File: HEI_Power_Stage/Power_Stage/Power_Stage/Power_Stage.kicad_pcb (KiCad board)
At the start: 4 copper layers, 114.7 x 57.4 mm, 151 parts, among them J1 OSTTA020161, J2 Conn_02x10_Odd_Even, J3 Screw_Terminal_01x01, J4 Screw_Terminal_01x01, J5 Screw_Terminal_01x01, Q1 EPC2304ENGRT, Q2 EPC2304ENGRT, Q3 EPC2304ENGRT, Q4 EPC2304ENGRT, Q5 EPC2304ENGRT, Q6 EPC2304ENGRT, T1 30k, T2 30k, T3 30k, T4 30k, T5 30k, T6 30k, U1 TBA 2-1212, U11 NCP51820AMNTWG, U12 ADC124S051CIMM/NOPB, U13 TPS73250DBVR, U14 TPS73250DBVR, U15 ADC124S051CIMM/NOPB, U17 TPS73250DBVR, U2 1769205241, U3 TPS73250DBVR, U5 NCP51820AMNTWG, U6 ADC124S051CIMM/NOPB, U8 NCP51820AMNTWG, U9 ADC124S051CIMM/NOPB

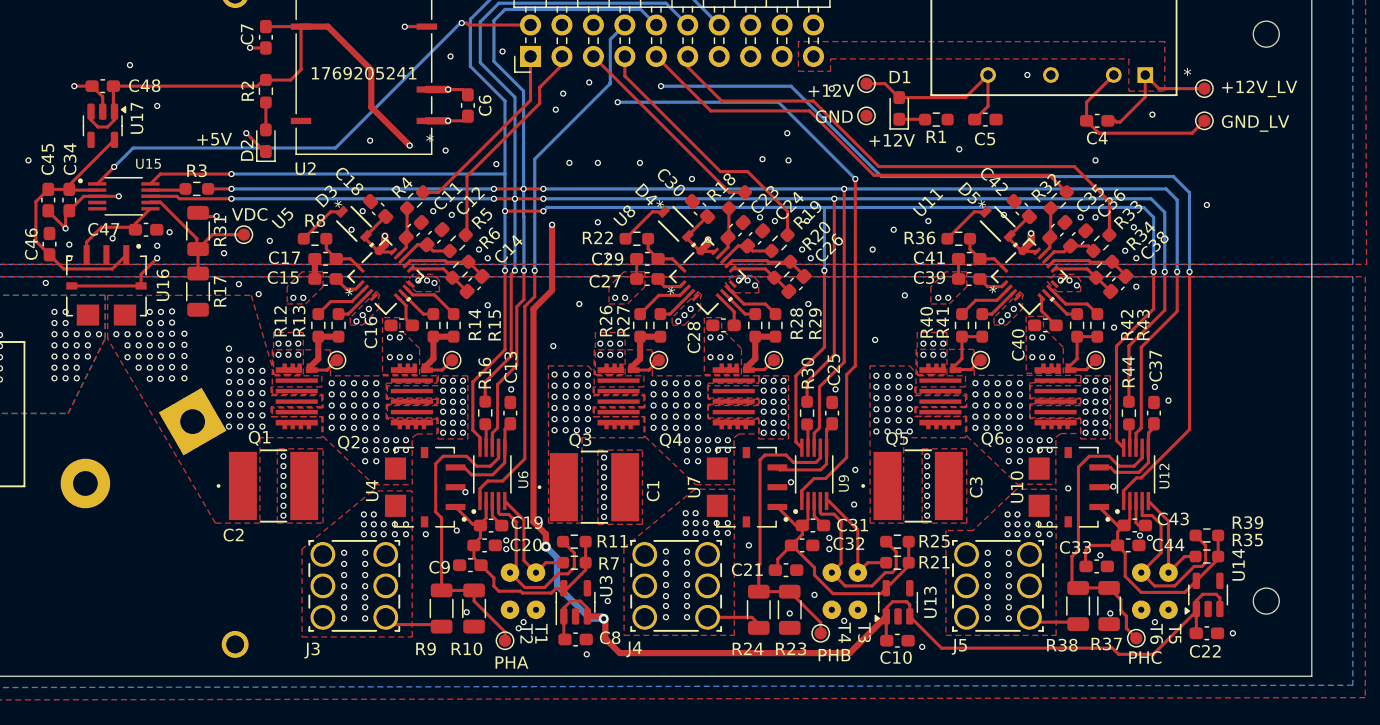
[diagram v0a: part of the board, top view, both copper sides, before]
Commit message: added low pass filters, PGND/SGND jumper
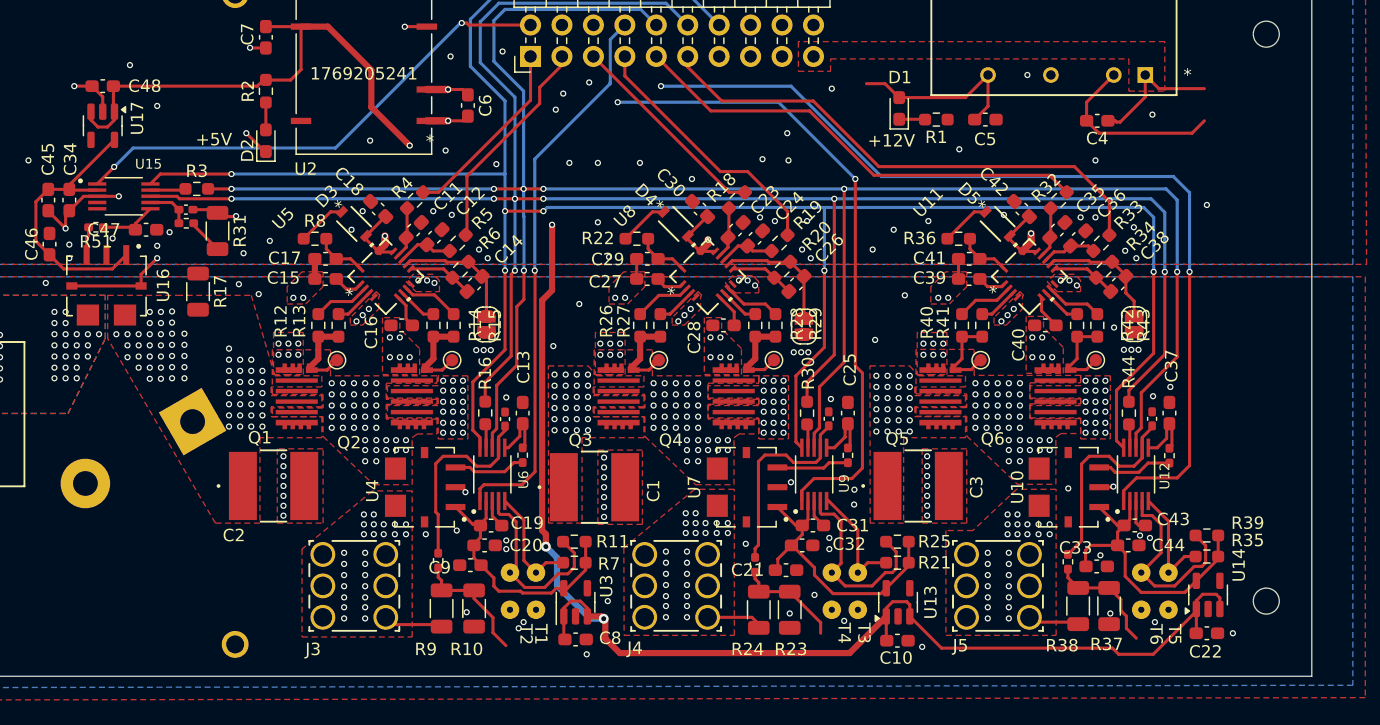
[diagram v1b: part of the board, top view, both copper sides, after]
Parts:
- removed +12V, +12V_LV, GND, GND_LV, PHA, PHB, PHC, VDC: Test_Point, TestPoint:TestPoint_Pad_D1.0mm
- added C54: 15pF, Capacitor_SMD:C_0402_1005Metric_Pad0.74x0.62mm_HandSolder, F.Cu at (126.5, 136.5)
- added C55: 15pF, Capacitor_SMD:C_0402_1005Metric_Pad0.74x0.62mm_HandSolder, F.Cu at (152.7, 136.5)
- added C56: 15pF, Capacitor_SMD:C_0402_1005Metric_Pad0.74x0.62mm_HandSolder, F.Cu at (178.8, 136.5)
- added C63: 15pF, Capacitor_SMD:C_0402_1005Metric_Pad0.74x0.62mm_HandSolder, F.Cu at (100.7, 119.6)
- added JP1: Jumper_2_Open, Jumper:SolderJumper-2_P1.3mm_Open_RoundedPad1.0x1.5mm, F.Cu at (125.0, 128.8)
- added JP2: Jumper_2_Open, Jumper:SolderJumper-2_P1.3mm_Open_RoundedPad1.0x1.5mm, F.Cu at (150.7, 129.0)
- added JP3: Jumper_2_Open, Jumper:SolderJumper-2_P1.3mm_Open_RoundedPad1.0x1.5mm, F.Cu at (177.3, 128.8)
- added R45: 2.2 0.1W, Resistor_SMD:R_0402_1005Metric_Pad0.72x0.64mm_HandSolder, F.Cu at (127.9, 139.4)
- added R46: 2.2 0.1W, Resistor_SMD:R_0402_1005Metric_Pad0.72x0.64mm_HandSolder, F.Cu at (154.2, 139.4)
- added R47: 2.2 0.1W, Resistor_SMD:R_0402_1005Metric_Pad0.72x0.64mm_HandSolder, F.Cu at (180.2, 139.4)
- added R48: 2.2 0.1W, Resistor_SMD:R_0402_1005Metric_Pad0.72x0.64mm_HandSolder, F.Cu at (121.1, 147.9)
- added R49: 2.2 0.1W, Resistor_SMD:R_0402_1005Metric_Pad0.72x0.64mm_HandSolder, F.Cu at (146.7, 148.3)
- added R50: 2.2 0.1W, Resistor_SMD:R_0402_1005Metric_Pad0.72x0.64mm_HandSolder, F.Cu at (172.0, 148.0)
- added R51: 2.2 0.1W, Resistor_SMD:R_0402_1005Metric_Pad0.72x0.64mm_HandSolder, F.Cu at (93.5, 121.0)
- added R57: 2.2 0.1W, Resistor_SMD:R_0402_1005Metric_Pad0.72x0.64mm_HandSolder, F.Cu at (100.8, 120.7)
- moved R31 1.58 mm to (103.3, 121.3)
- moved C25 1.28 mm to (154.2, 136.0)
- moved C37 1.25 mm to (180.2, 136.0)
- moved C13 1.00 mm to (127.9, 136.0)
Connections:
- C13 pad 1: /Phase1/I_{sense} -> /Phase1/I_{ADC}
- C25 pad 1: /Phase2/I_{sense} -> /Phase2/I_{ADC}
- C37 pad 1: /Phase3/I_{sense} -> /Phase3/I_{ADC}
- C46 pad 2: GND -> GNDPWR
- C47 pad 1: /DCI_{sense} -> /I_{DC}
- C47 pad 2: GND -> GNDPWR
- U12 pad 6: /Phase3/I_{sense} -> /Phase3/I_{ADC}
- U12 pad 7: /Phase3/V_{sense} -> /Phase3/V_{ADC}
- U15 pad 6: /DCI_{sense} -> /I_{DC}
- U15 pad 7: /DCV_{sense} -> /V_{DC}
- U16 pad 2: GND -> GNDPWR
- U16 pad 4: GND -> GNDPWR
- U16 pad 7: GND -> GNDPWR
- U6 pad 6: /Phase1/I_{sense} -> /Phase1/I_{ADC}
- U6 pad 7: /Phase1/V_{sense} -> /Phase1/V_{ADC}
- U9 pad 6: /Phase2/I_{sense} -> /Phase2/I_{ADC}
- U9 pad 7: /Phase2/V_{sense} -> /Phase2/V_{ADC}
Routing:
- net /Phase3/V_{ADC}: track 0.00 -> 16.5 mm
- net /Phase2/V_{ADC}: track 0.00 -> 16.4 mm
- net /Phase1/V_{ADC}: track 0.00 -> 16.0 mm
- net /Phase3/V_{sense}: track 24.7 -> 9.43 mm
- net /Phase2/V_{sense}: track 24.3 -> 9.01 mm
- net /Phase1/V_{sense}: track 24.9 -> 10.1 mm
- net GNDPWR: track 28.4 -> 38.9 mm, vias 184 -> 190
- net /DCV_{sense}: track 12.4 -> 2.89 mm
- net /DCI_{sense}: track 7.77 -> 2.30 mm
- net /Phase3/I_{ADC}: track 0.00 -> 5.20 mm
- net /Phase2/I_{ADC}: track 0.00 -> 5.12 mm
- net /I_{DC}: track 0.00 -> 4.88 mm
- net /Phase1/I_{ADC}: track 0.00 -> 4.79 mm
- net /V_{DC}: track 0.00 -> 3.65 mm
- net /Phase1/I_{sense}: track 7.96 -> 5.88 mm
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
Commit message: spi isolation
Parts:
- moved R17 1.60 mm to (103.3, 126.2)
- moved C49 0.17 mm to (104.8, 102.1)
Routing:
- net /Phase1/V_{sense}: track 10.1 -> 4.55 mm
- net /Phase3/V_{sense}: track 9.43 -> 4.46 mm
- net /Phase2/V_{sense}: track 9.01 -> 4.62 mm
- net GNDPWR: track 38.9 -> 42.3 mm, vias 190 -> 192
- net /DCV_{sense}: track 2.89 -> 4.87 mm
- net GND: vias 41 -> 40
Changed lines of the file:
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@@
 		(tags "capacitor handsolder")
 		(property "Reference" "C55"
-			(at 0 -1.16 270)
+			(at 0 -1.16 -90)
 			(layer "F.SilkS")
 			(hide yes)
@@
 		)
 		(property "Value" "15pF"
-			(at 0 1.16 270)
+			(at 0 1.16 -90)
 			(layer "F.Fab")
 			(effects
@@
 		)
 		(fp_text user "${REFERENCE}"
-			(at 0 0 270)
+			(at 0 0 -90)
 			(layer "F.Fab")
 			(effects
@@
 		(tags "capacitor handsolder")
 		(property "Reference" "C56"
-			(at 0 -1.16 270)
+			(at 0 -1.16 -90)
 			(layer "F.SilkS")
 			(hide yes)
@@
 		)
 		(property "Value" "15pF"
-			(at 0 1.16 270)
+			(at 0 1.16 -90)
 			(layer "F.Fab")
 			(effects
@@
 		)
 		(fp_text user "${REFERENCE}"
-			(at 0 0 270)
+			(at 0 0 -90)
 			(layer "F.Fab")
 			(effects
@@
 	(footprint "Resistor_SMD:R_1206_3216Metric"
 		(layer "F.Cu")
-		(at 101.7 126.2 -90)
+		(at 103.3 126.2 -90)
 		(descr "Resistor SMD 1206 (3216 Metric), square (rectangular) end terminal, IPC_7351 nominal, (Body size source: IPC-SM-782 page 72, https://www.pcb-3d.com/wordpress/wp-content/uploads/ipc-sm-782a_amendment_1_and_2.pdf), generated with kicad-footprint-generator")
 		(tags "resistor")
@@
 	(footprint "kemet_cap:C4AQLEW6210A3BK"
 		(layer "B.Cu")
-		(at 104.7 102.2 -90)
+		(at 104.85 102.125 -90)
 		(descr "C4AQLEW6210A3BK-2")
 		(tags "Capacitor")
@@
 	)
 	(segment
+		(start 94.3 122.1)
+		(end 94.3 123.240788)
+		(width 0.25)
+		(layer "F.Cu")
+		(net 2)
+	)
+	(segment
 		(start 97.1 124.8)
 		(end 97.1 125.740788)
@@
 	)
 	(segment
+		(start 94.5 121.9)
+		(end 94.3 122.1)
+		(width 0.25)
+		(layer "F.Cu")
+		(net 2)
+	)
+	(segment
 		(start 94 111.6625)
 		(end 94 110.4625)
@@
 	)
 	(segment
+		(start 94.8 121.9)
+		(end 94.5 121.9)
+		(width 0.25)
+		(layer "F.Cu")
+		(net 2)
+	)
+	(segment
 		(start 103.0125 119.575)
 		(end 103.275 119.8375)
@@
 	)
 	(segment
+		(start 99.4625 122.3)
+		(end 98.3625 121.2)
+		(width 0.25)
+		(layer "F.Cu")
+		(net 2)
+	)
+	(segment
 		(start 177.474999 144.86565)
 		(end 177.699999 145.09065)
@@
 	)
 	(segment
+		(start 99.6 122.3)
+		(end 99.4625 122.3)
+		(width 0.25)
+		(layer "F.Cu")
+		(net 2)
+	)
+	(segment
 		(start 105.915 106.515)
 		(end 105.9 106.5)
@@
 	)
 	(via
+		(at 99.6 122.3)
+		(size 0.5)
+		(drill 0.3)
+		(layers "F.Cu" "B.Cu")
+		(free yes)
+		(net 2)
+	)
+	(via
 		(at 148.2 134.2)
 		(size 0.5)
@@
 	)
 	(via
-		(at 106.6 126.4)
+		(at 107 125.7)
 		(size 0.5)
 		(drill 0.3)
@@
 	)
 	(via
+		(at 94.8 121.9)
+		(size 0.5)
+		(drill 0.3)
+		(layers "F.Cu" "B.Cu")
+		(free yes)
+		(net 2)
+	)
+	(via
 		(at 152.7 146.1)
 		(size 0.5)
@@
 	)
 	(via
-		(at 94.8 121.9)
-		(size 0.5)
-		(drill 0.3)
-		(layers "F.Cu" "B.Cu")
-		(free yes)
-		(net 5)
-	)
-	(via
 		(at 91.3 122.4)
 		(size 0.5)
@@
 	)
 	(via
-		(at 99.4 121.4)
+		(at 100.9 121.8)
 		(size 0.5)
 		(drill 0.3)
@@
 	)
 	(segment
-		(start 127.45 132.15)
-		(end 127.45 127.413604)
+		(start 177.9 137.215876)
+		(end 177.9 134.375)
 		(width 0.25)
 		(layer "F.Cu")
@@
 	)
 	(segment
-		(start 177.9 137.215876)
-		(end 177.9 134.375)
+		(start 125.475002 138.815)
+		(end 125.475002 137.627074)
 		(width 0.25)
 		(layer "F.Cu")
@@
 	)
 	(segment
+		(start 128.025 131.575)
+		(end 128.025 124.5)
+		(width 0.25)
+		(layer "F.Cu")
+		(net 19)
+	)
+	(segment
 		(start 177.474999 137.640877)
 		(end 177.9 137.215876)
@@
 	)
 	(segment
-		(start 127.45 127.413604)
-		(end 128.025 126.838604)
+		(start 125.825 133.775)
+		(end 128.025 131.575)
 		(width 0.25)
 		(layer "F.Cu")
@@
 	)
 	(segment
-		(start 125.825 137.277076)
-		(end 125.825 133.775)
-		(width 0.25)
-		(layer "F.Cu")
-		(net 19)
-	)
-	(segment
-		(start 125.475002 138.815)
-		(end 125.475002 137.627074)
-		(width 0.25)
-		(layer "F.Cu")
-		(net 19)
-	)
-	(segment
-		(start 125.825 133.775)
-		(end 127.45 132.15)
-		(width 0.25)
-		(layer "F.Cu")
-		(net 19)
-	)
-	(segment
 		(start 125.6 117.9)
 		(end 128 117.9)
@@
 	)
 	(segment
-		(start 151.475 137.640876)
-		(end 151.475 138.815)
+		(start 125.825 137.277076)
+		(end 125.825 133.775)
 		(width 0.25)
 		(layer "F.Cu")
@@
 	)
 	(segment
-		(start 128.025 126.838604)
-		(end 128.025 124.5)
+		(start 151.475 137.640876)
+		(end 151.475 138.815)
 		(width 0.25)
 		(layer "F.Cu")
@@
 	)
 	(segment
-		(start 127 131.4)
-		(end 127 124.8)
+		(start 125.6 118.7)
+		(end 127.3 118.7)
 		(width 0.25)
 		(layer "F.Cu")
@@
 	)
 	(segment
-		(start 125.6 118.7)
-		(end 127.3 118.7)
+		(start 127.3 131.1)
+		(end 127.3 124.5)
 		(width 0.25)
 		(layer "F.Cu")
@@
 	)
 	(segment
-		(start 127 124.8)
-		(end 127.3 124.5)
-		(width 0.25)
-		(layer "F.Cu")
-		(net 21)
-	)
-	(segment
 		(start 124.9 133.5)
-		(end 127 131.4)
-		(width 0.25)
-		(layer "F.Cu")
-		(net 21)
-	)
-	(segment
-		(start 124.9 135.0875)
-		(end 124.9 133.5)
+		(end 127.3 131.1)
 		(width 0.25)
 		(layer "F.Cu")
@@
 		(net 21)
 	)
+	(segment
+		(start 124.9 135.0875)
+		(end 124.9 133.5)
+		(width 0.25)
+		(layer "F.Cu")
+		(net 21)
+	)
 	(via
 		(at 127.3 124.5)
@@
 	)
 	(segment
-		(start 125.525 153.75)
-		(end 126.575 154.8)
-		(width 0.25)
-		(layer "F.Cu")
-		(net 64)
-	)
-	(segment
-		(start 125.525 152.525)
-		(end 125.525 153.75)
-		(width 0.25)
-		(layer "F.Cu")
-		(net 64)
-	)
-	(segment
-		(start 124 150.3375)
-		(end 124 151)
-		(width 0.25)
-		(layer "F.Cu")
-		(net 64)
-	)
-	(segment
-		(start 124 151)
-		(end 125.525 152.525)
-		(width 0.25)
-		(layer "F.Cu")
-		(net 64)
-	)
-	(segment
 		(start 121.375002 150.3375)
 		(end 121.375002 149.550002)
@@
 	)
 	(segment
-		(start 149.5 150.4375)
-		(end 152 152.9375)
-		(width 0.25)
-		(layer "F.Cu")
-		(net 71)
-	)
-	(segment
 		(start 146.7 149.4)
 		(end 146.7 148.87)
@@
 	)
 	(segment
-		(start 152 152.9375)
-		(end 152 153.8)
-		(width 0.25)
-		(layer "F.Cu")
-		(net 71)
-	)
-	(segment
 		(start 147 150.1375)
 		(end 147.3 150.4375)
@@
 	)
 	(segment
-		(start 176.7 153.4)
-		(end 177.5 154.2)
-		(width 0.25)
-		(layer "F.Cu")
-		(net 78)
-	)
-	(segment
-		(start 176.252944 151.090444)
-		(end 176.252944 151.975)
-		(width 0.25)
-		(layer "F.Cu")
-		(net 78)
-	)
-	(segment
-		(start 176.7 152.422056)
-		(end 176.7 153.4)
-		(width 0.25)
-		(layer "F.Cu")
-		(net 78)
-	)
-	(segment
 		(start 172.8 150.1375)
 		(end 175.4 150.1375)
@@
 	)
 	(segment
-		(start 176.252944 151.975)
-		(end 176.7 152.422056)
-		(width 0.25)
-		(layer "F.Cu")
-		(net 78)
-	)
-	(segment
 		(start 172.8 150.1375)
 		(end 171.975 149.3125)
@@
 	)
 	(segment
-		(start 175.3 150.1375)
-		(end 176.252944 151.090444)
-		(width 0.25)
-		(layer "F.Cu")
-		(net 78)
-	)
-	(segment
 		(start 178.777075 144.29065)
 		(end 179.5 145.013575)
@@
 	)
 	(segment
+		(start 103.275 122.7625)
+		(end 103.275 124.7125)
+		(width 0.25)
+		(layer "F.Cu")
+		(net 93)
+	)
+	(segment
 		(start 101.3475 120.835)
 		(end 101.3475 120.675)
 		(width 0.25)
 		(layer "F.Cu")
+		(net 93)
+	)
+	(segment
+		(start 103.275 124.7125)
+		(end 103.3 124.7375)
+		(width 0.25)
+		(layer "F.Cu")

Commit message: small changes
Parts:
- added C4: 10uF, Capacitor_SMD:C_0603_1608Metric_Pad1.08x0.95mm_HandSolder, F.Cu at (169.0, 63.1)
- added C5: 10uF, Capacitor_SMD:C_0603_1608Metric_Pad1.08x0.95mm_HandSolder, F.Cu at (169.0, 65.6)
- added C51: 10uF, Capacitor_SMD:C_0603_1608Metric_Pad1.08x0.95mm_HandSolder, F.Cu at (179.7, 63.1)
- added C52: 10uF, Capacitor_SMD:C_0603_1608Metric_Pad1.08x0.95mm_HandSolder, F.Cu at (179.7, 65.6)
- added D1: G, LED_SMD:LED_0603_1608Metric_Pad1.05x0.95mm_HandSolder, F.Cu at (164.7, 80.5)
- added R1: 1.8k, Resistor_SMD:R_0603_1608Metric_Pad0.98x0.95mm_HandSolder, F.Cu at (169.0, 68.1)
- added TP1: Test_Point, TestPoint:TestPoint_Keystone_5000-5004_Miniature, F.Cu at (164.7, 64.0)
- added TP11: Test_Point, TestPoint:TestPoint_Keystone_5000-5004_Miniature, F.Cu at (175.4, 64.0)
- added TP12: Test_Point, TestPoint:TestPoint_Keystone_5000-5004_Miniature, F.Cu at (175.4, 68.3)
- added TP2: Test_Point, TestPoint:TestPoint_Keystone_5000-5004_Miniature, F.Cu at (164.7, 68.3)
- added TP3: Test_Point, TestPoint:TestPoint_Keystone_5000-5004_Miniature, F.Cu at (164.7, 72.7)
- added TP4: Test_Point, TestPoint:TestPoint_Keystone_5000-5004_Miniature, F.Cu at (164.7, 77.0)
- added U18: ISO6741, Package_SO:SOIC-16W_7.5x10.3mm_P1.27mm, F.Cu at (156.1, 67.8)
- added U19: ISO6741, Package_SO:SOIC-16W_7.5x10.3mm_P1.27mm, F.Cu at (156.1, 79.8)
- added U20: ISO6760, iso6760:SOIC16_ISO6760_DW_TEX, F.Cu at (176.7, 80.1)
- added U21: 1769205241, GTSR:176920512, F.Cu at (107.6, 86.7)
- U1: footprint GTSR_KiCAD_Footprints_SD:TBA 2_SINGLE_TRP -> GTSR:TBA 2_SINGLE_TRP
- moved U1 24.7 mm to (190.9, 87.5), turned to 0 degrees
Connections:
- net VDC renamed HV+
- net VDCin renamed HV+in
- C1 pad 2: GNDPWR -> HV-
- C10 pad 1: +5V -> +5V_HV
- C10 pad 2: GNDPWR -> HV-
- C13 pad 2: GNDPWR -> HV-
- C16 pad 1: GNDPWR -> HV-
- C19 pad 2: GNDPWR -> HV-
- C2 pad 2: GNDPWR -> HV-
- C20 pad 2: GNDPWR -> HV-
- C21 pad 2: GNDPWR -> HV-
- C22 pad 1: +5V -> +5V_HV
- C22 pad 2: GNDPWR -> HV-
- C25 pad 2: GNDPWR -> HV-
- C28 pad 1: GNDPWR -> HV-
- C3 pad 2: GNDPWR -> HV-
- C31 pad 2: GNDPWR -> HV-
- C32 pad 2: GNDPWR -> HV-
- C33 pad 2: GNDPWR -> HV-
- C34 pad 2: GNDPWR -> HV-
- C37 pad 2: GNDPWR -> HV-
- C40 pad 1: GNDPWR -> HV-
- C43 pad 2: GNDPWR -> HV-
- C44 pad 2: GNDPWR -> HV-
- C45 pad 2: GNDPWR -> HV-
- C46 pad 2: GNDPWR -> HV-
- C47 pad 2: GNDPWR -> HV-
- C48 pad 1: +5V -> +5V_HV
- C48 pad 2: GNDPWR -> HV-
- C49 pad 1: GNDPWR -> HV-
- C49 pad 4: GNDPWR -> HV-
- C50 pad 2: GNDPWR -> HV-
- C54 pad 2: GNDPWR -> HV-
- C55 pad 2: GNDPWR -> HV-
- C56 pad 2: GNDPWR -> HV-
- C6 pad 1: +12V_LV -> +12V
- C6 pad 2: /GND_LV -> GND
- C63 pad 2: GNDPWR -> HV-
- C7 pad 1: +5V -> +5V_HV
- C7 pad 2: GNDPWR -> HV-
- C8 pad 1: +5V -> +5V_HV
- C8 pad 2: GNDPWR -> HV-
- C9 pad 2: GNDPWR -> HV-
- D2 pad 1: GNDPWR -> HV-
- J1 pad 2: GNDPWR -> HV-
- J2 pad 1: /AHS_{PWM} -> /AHS_{PWM}_LV
- J2 pad 10: /MOSI -> /MOSI_LV
- J2 pad 11: /CLS_{PWM} -> /CLS_{PWM}_LV
- J2 pad 12: /MISO -> /MISO_LV
- J2 pad 14: /CLK -> /CLK_LV
- J2 pad 16: +5V -> unconnected-(J2-Pin_16-Pad16)
- J2 pad 17: GND -> unconnected-(J2-Pin_17-Pad17)
- J2 pad 18: GNDPWR -> +3V3_LV
- J2 pad 19: +12V_LV -> /12V_LV
- J2 pad 2: /DC~{CS} -> /DC~{CS}_LV
- J2 pad 3: /ALS_{PWM} -> /ALS_{PWM}_LV
- J2 pad 4: /C~{CS} -> /C~{CS}_LV
- J2 pad 5: /BHS_{PWM} -> /BHS_{PWM}_LV
- J2 pad 6: /B~{CS} -> /B~{CS}_LV
- J2 pad 7: /BLS_{PWM} -> /BLS_{PWM}_LV
- J2 pad 8: /A~{CS} -> /A~{CS}_LV
- J2 pad 9: /CHS_{PWM} -> /CHS_{PWM}_LV
- JP1 pad 2: GNDPWR -> HV-
- JP2 pad 2: GNDPWR -> HV-
- JP3 pad 2: GNDPWR -> HV-
- Q2 pad 2: GNDPWR -> HV-
- Q2 pad 4: GNDPWR -> HV-
- Q2 pad 6: GNDPWR -> HV-
- Q4 pad 2: GNDPWR -> HV-
- Q4 pad 4: GNDPWR -> HV-
- Q4 pad 6: GNDPWR -> HV-
- Q6 pad 2: GNDPWR -> HV-
- Q6 pad 4: GNDPWR -> HV-
- Q6 pad 6: GNDPWR -> HV-
- R10 pad 1: GNDPWR -> HV-
- R2 pad 2: +5V -> +5V_HV
- R24 pad 1: GNDPWR -> HV-
- R31 pad 1: GNDPWR -> HV-
- R38 pad 1: GNDPWR -> HV-
- T1 pad 2: GNDPWR -> HV-
- T2 pad 2: GNDPWR -> HV-
- T3 pad 2: GNDPWR -> HV-
- T4 pad 2: GNDPWR -> HV-
- T5 pad 2: GNDPWR -> HV-
- T6 pad 2: GNDPWR -> HV-
- U1 pad 1: +12V_LV -> /12V_LV
- U10 pad 2: GNDPWR -> HV-
- U10 pad 4: GNDPWR -> HV-
- U10 pad 7: GNDPWR -> HV-
- U11 pad 8: GNDPWR -> HV-
- U12 pad 3: GNDPWR -> HV-
- U13 pad 1: +5V -> +5V_HV
- U13 pad 2: GNDPWR -> HV-
- U13 pad 3: +5V -> +5V_HV
- U14 pad 1: +5V -> +5V_HV
- U14 pad 2: GNDPWR -> HV-
- U14 pad 3: +5V -> +5V_HV
- U15 pad 3: GNDPWR -> HV-
- U16 pad 2: GNDPWR -> HV-
- U16 pad 4: GNDPWR -> HV-
- U16 pad 7: GNDPWR -> HV-
- U17 pad 1: +5V -> +5V_HV
- U17 pad 2: GNDPWR -> HV-
- U17 pad 3: +5V -> +5V_HV
- U2 pad 1: /GND_LV -> GND
- U2 pad 2: +12V_LV -> +12V
- U2 pad 4: GNDPWR -> HV-
- U2 pad 5: +5V -> +5V_HV
- U3 pad 1: +5V -> +5V_HV
- U3 pad 2: GNDPWR -> HV-
- U3 pad 3: +5V -> +5V_HV
- U4 pad 2: GNDPWR -> HV-
- U4 pad 4: GNDPWR -> HV-
- U4 pad 7: GNDPWR -> HV-
- U5 pad 8: GNDPWR -> HV-
- U6 pad 3: GNDPWR -> HV-
- U7 pad 2: GNDPWR -> HV-
- U7 pad 4: GNDPWR -> HV-
- U7 pad 7: GNDPWR -> HV-
- U8 pad 8: GNDPWR -> HV-
- U9 pad 3: GNDPWR -> HV-
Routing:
- net GNDPWR: track 42.3 -> 0.00 mm, vias 192 -> 0
- net HV-: track 0.00 -> 42.3 mm, vias 0 -> 190
- net GND: vias 40 -> 42
- net +12V_LV: vias 1 -> 0
- net +12V: vias 3 -> 4
- added copper zone on B.Cu, net +3V3_LV
- added copper zone on F.Cu, net /12V_LV
- added copper zone on F.Cu, net HV-
- added copper zone on In1.Cu, net HV-
- added copper zone on In2.Cu, net HV-
- removed copper zone on F.Cu, net +12V_LV
- removed copper zone on B.Cu, net GNDPWR
- removed copper zone on F.Cu, net GNDPWR
- removed copper zone on In1.Cu, net GNDPWR
- removed copper zone on In2.Cu, net GNDPWR

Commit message: git ignore pls work
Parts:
- added J6: Screw_Terminal_01x01, GTSR:CONN6_1057_WRE, F.Cu at (79.6, 138.0)
- J1: value OSTTA020161 -> Screw_Terminal_01x01; footprint GTSR_KiCAD_Footprints:CONN_OSTTA020161_OST -> GTSR:CONN6_1057_WRE
- moved J1 6.48 mm to (79.2, 127.9), turned to 0 degrees
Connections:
- J1 pad 2: HV- -> HV+in
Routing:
- net HV-: vias 190 -> 188
